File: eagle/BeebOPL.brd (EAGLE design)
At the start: 100 x 80 mm, 46 parts, among them IC1 LM324N, IC2 YM3014B, IC3 7805TV, IC5 74LS02N, IC6 YM3812, IC7 74LS04N, IC9 74HCT688N, J1 1 MHz Bus, J2 Feed-through, J3 3.5mm Jack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

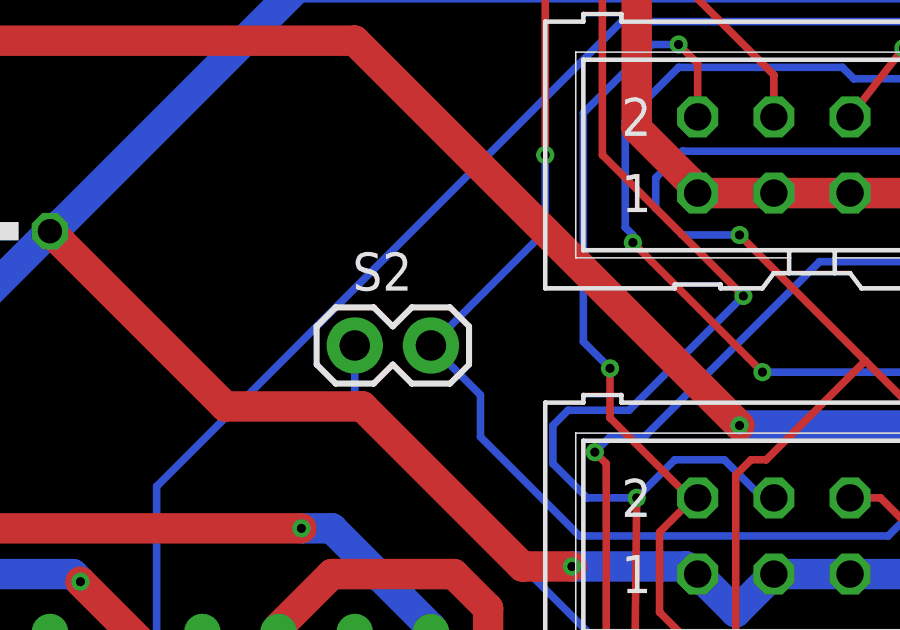
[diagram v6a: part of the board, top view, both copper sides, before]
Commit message: Set IRQ as connected by default
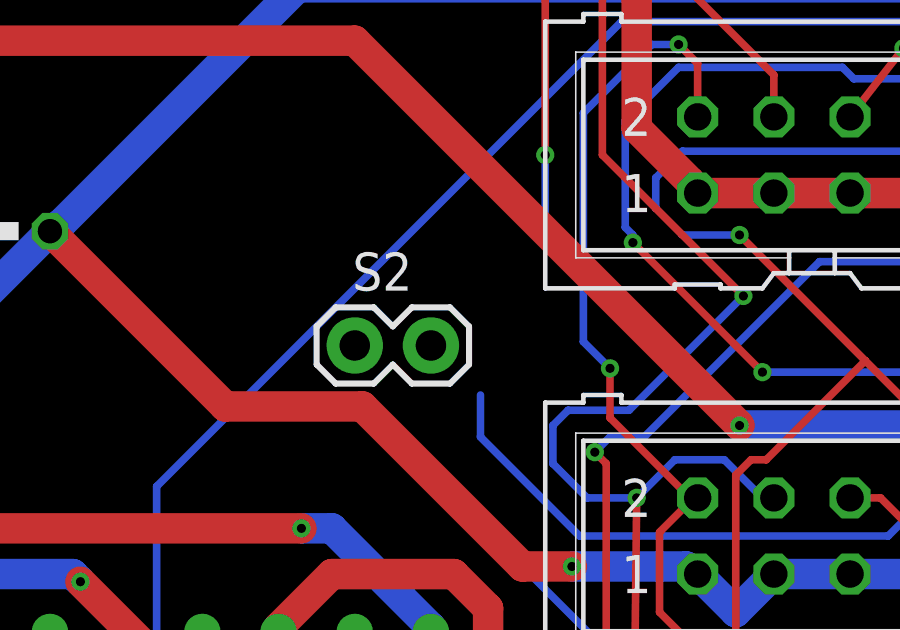
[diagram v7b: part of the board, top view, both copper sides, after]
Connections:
- net /IRQ: now also S2.1
- net YM/IRQ: no longer S2.1
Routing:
- net /IRQ: track 52.9 -> 45.1 mm
- net YM/IRQ: track 50.3 -> 48.5 mm
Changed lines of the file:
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@@
 <contactref element="J1" pad="8"/>
 <contactref element="J2" pad="8"/>
-<contactref element="S2" pad="2"/>
-<wire x1="43.18" y1="66.04" x2="44.831" y2="64.389" width="0.254" layer="16"/>
 <wire x1="44.831" y1="64.389" x2="44.831" y2="62.992" width="0.254" layer="16"/>
 <wire x1="44.831" y1="62.992" x2="48.133" y2="59.69" width="0.254" layer="16"/>
@@
 <wire x1="60.706" y1="76.962" x2="59.69" y2="77.978" width="0.254" layer="1"/>
 <wire x1="46.99" y1="69.85" x2="46.99" y2="72.39" width="0.254" layer="16"/>
-<wire x1="43.18" y1="66.04" x2="46.99" y2="69.85" width="0.254" layer="16"/>
 <via x="46.99" y="72.39" extent="1-16" drill="0.3048"/>
 <wire x1="46.99" y1="77.724" x2="46.99" y2="72.39" width="0.254" layer="1"/>
@@
 <wire x1="48.641" y1="79.375" x2="51.562" y2="79.375" width="0.2286" layer="1"/>
 <wire x1="51.562" y1="79.375" x2="52.959" y2="77.978" width="0.2286" layer="1"/>
+<contactref element="S2" pad="1"/>
+<contactref element="S2" pad="2"/>
+<wire x1="43.18" y1="66.04" x2="46.99" y2="69.85" width="0" layer="19" extent="16-16"/>
+<wire x1="44.831" y1="64.389" x2="43.18" y2="66.04" width="0" layer="19" extent="16-16"/>
+<wire x1="40.64" y1="66.04" x2="43.18" y2="66.04" width="0" layer="19" extent="1-1"/>
 </signal>
 <signal name="/NMI">
@@
 <signal name="YM/IRQ">
 <contactref element="IC6" pad="/IRQ"/>
-<contactref element="S2" pad="1"/>
 <wire x1="40.64" y1="64.262" x2="49.5935" y2="55.3085" width="0.254" layer="16"/>
-<wire x1="40.64" y1="66.04" x2="40.64" y2="64.262" width="0.254" layer="16"/>
 <wire x1="57.15" y1="24.13" x2="59.055" y2="26.035" width="0.254" layer="16"/>
 <wire x1="59.055" y1="26.035" x2="59.055" y2="31.115" width="0.254" layer="16"/>

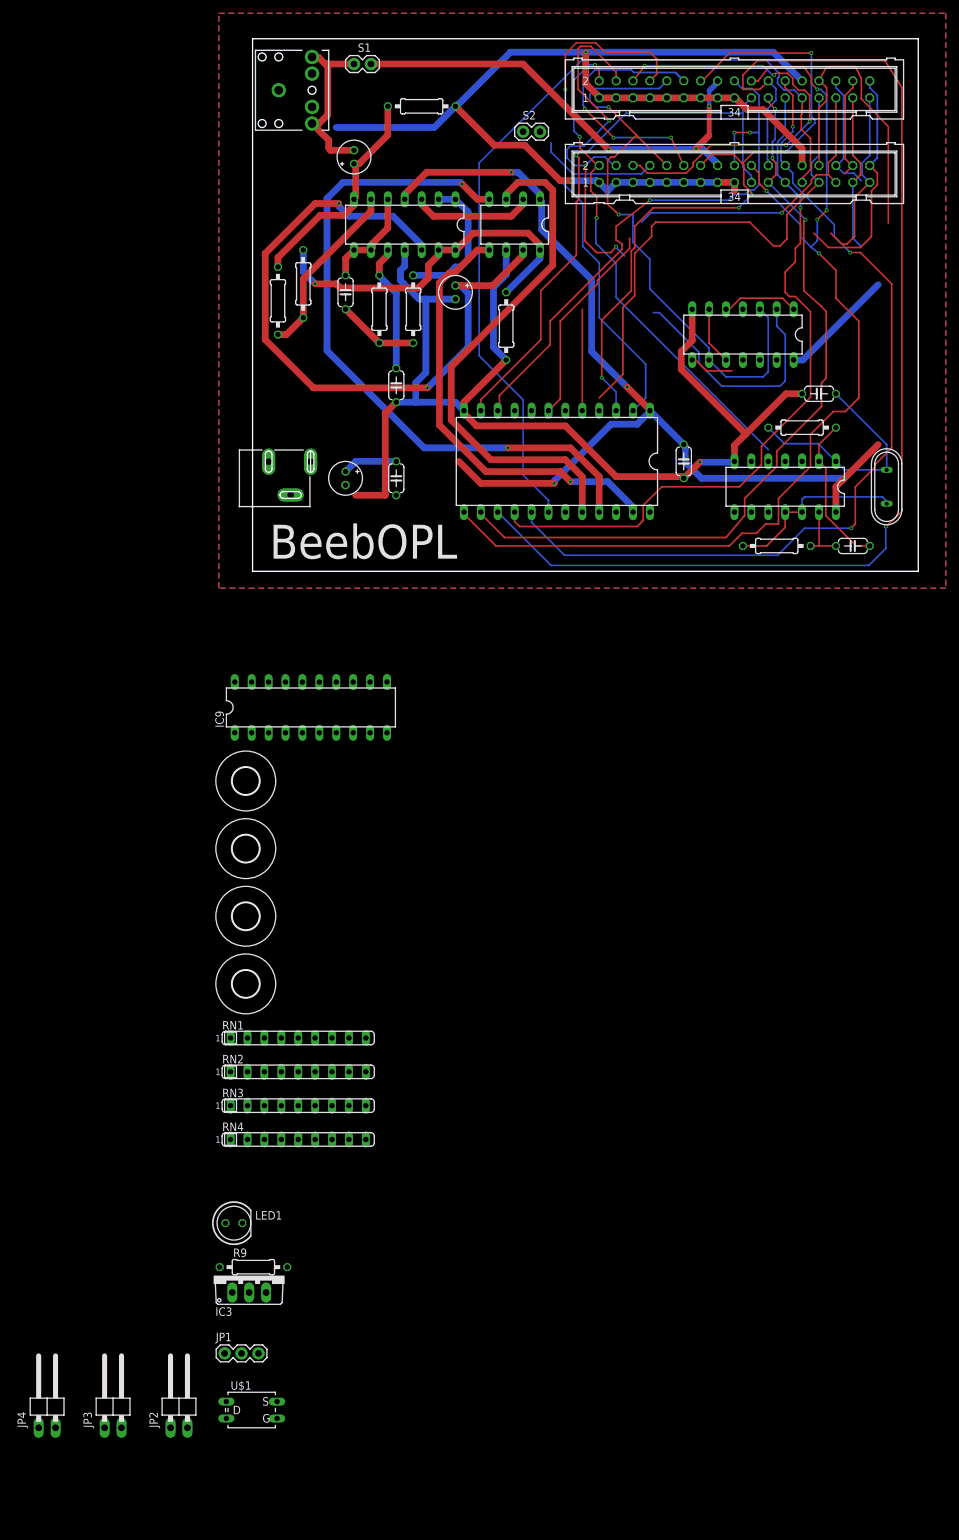
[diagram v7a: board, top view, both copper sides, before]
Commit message: Tidied-up schematic
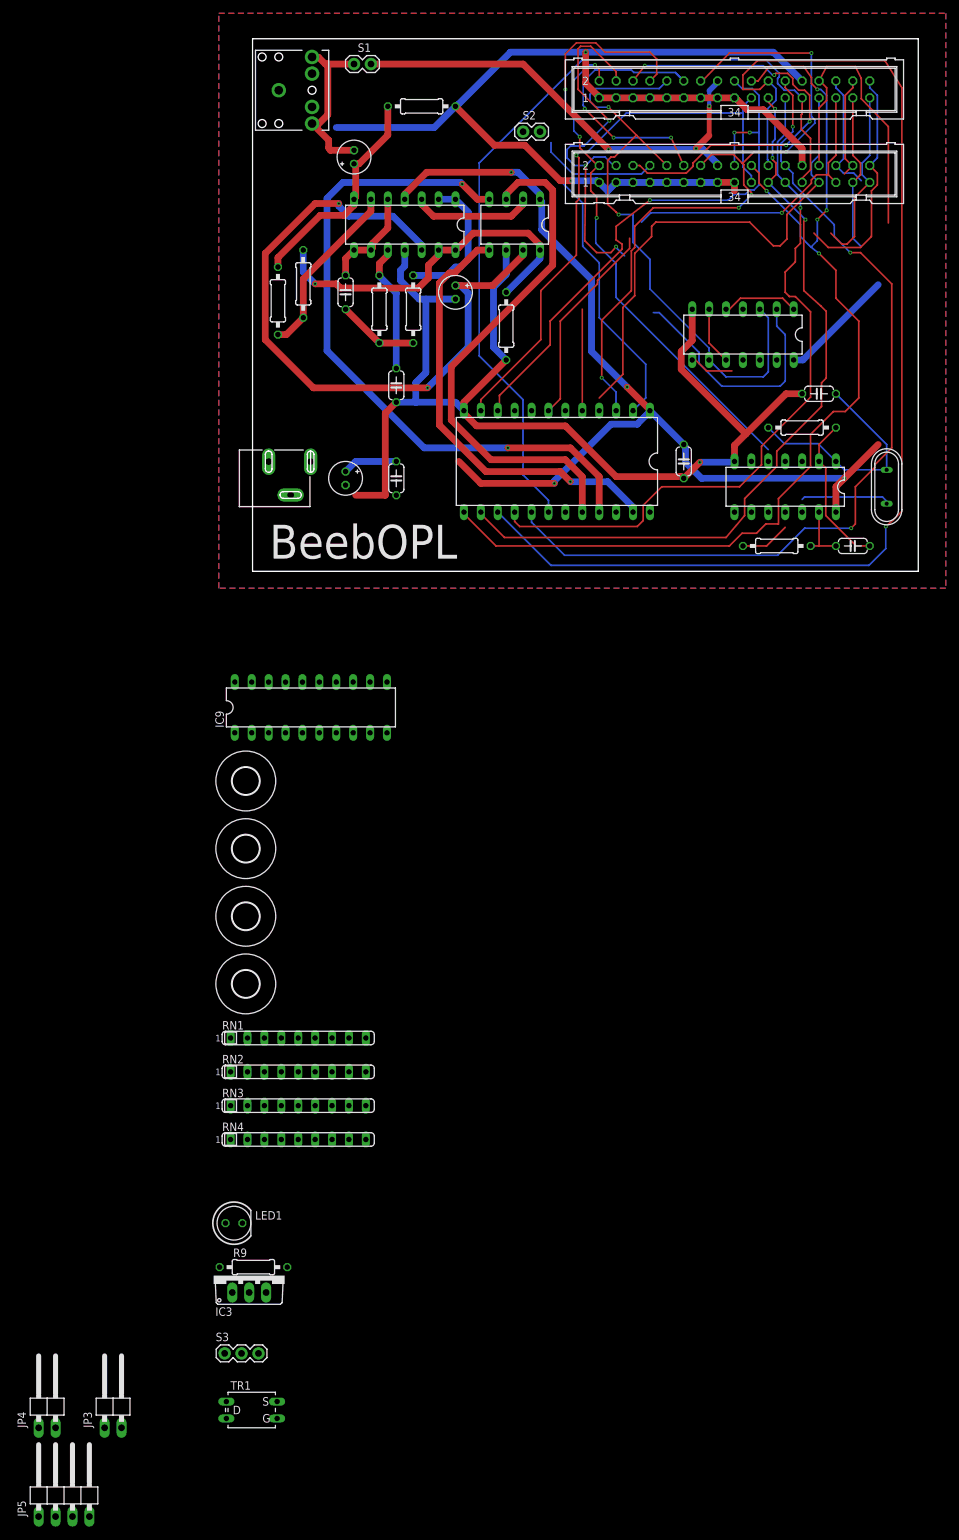
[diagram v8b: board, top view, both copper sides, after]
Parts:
- removed JP2: (no value), pinhead:1X02/90
- added JP5: (no value), pinhead:1X04/90
- IC3: value 7805TV -> LM7805
- RN1, RN2, RN3, RN4: value 2K2 -> 2k2
- S3: value JUMPER-3PTH -> (none)
- renumbered JP1 to S3, U$1 to TR1
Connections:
- removed net YM/IRQ: IC6./IRQ
- net /IRQ: now also IC6./IRQ
- net GND: now also JP5.2, JP5.3; no longer JP2.2
- net VCC: now also JP5.4; no longer JP2.1
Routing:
- net YM/IRQ: track 48.5 -> 0.00 mm
- net /IRQ: track 45.1 -> 93.7 mm
- net N$28: track 27.7 -> 21.0 mm
